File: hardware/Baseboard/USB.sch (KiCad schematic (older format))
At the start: 9 parts, among them IC9 FT232RL, X2 SERIAL

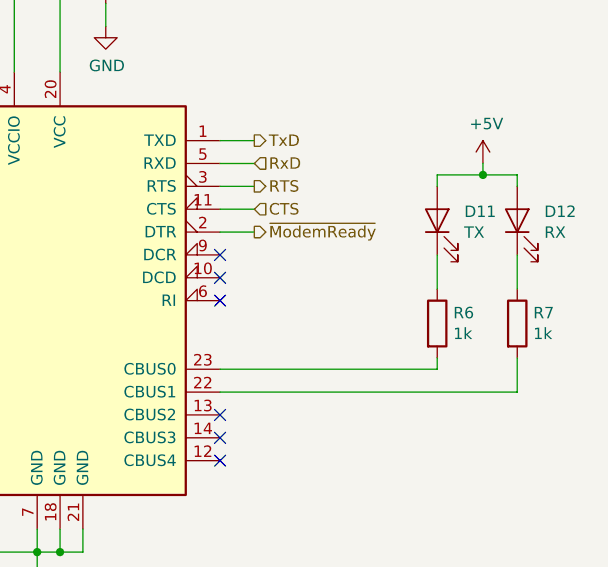
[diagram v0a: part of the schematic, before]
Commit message: Rework hardware for IRQ, change some routing
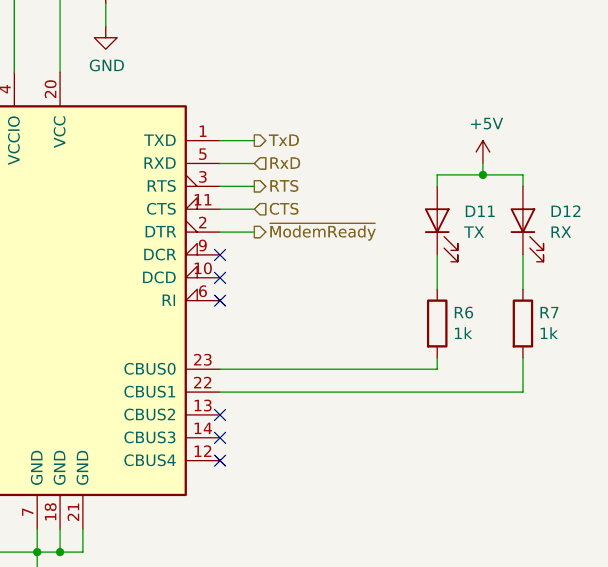
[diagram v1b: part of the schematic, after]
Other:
- moved on the sheet: D12, R7

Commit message: Working on PCB
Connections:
- net ~DSR: now reaches IC9.9 (DCR)
- net CTS renamed ~CTS
- net RTS renamed ~RTS
- net ~ModemReady renamed ~DTR
- net ~Reset renamed ~Reset_FT232
- no-connect marks 10 -> 9
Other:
- moved on the sheet: C14, C15, C16, D11, D12, R6, R7
